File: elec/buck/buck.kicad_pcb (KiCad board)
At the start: 2 copper layers, 33 x 27.9 mm, 14 parts, among them J1 Conn_01x08, J2 Conn_01x08

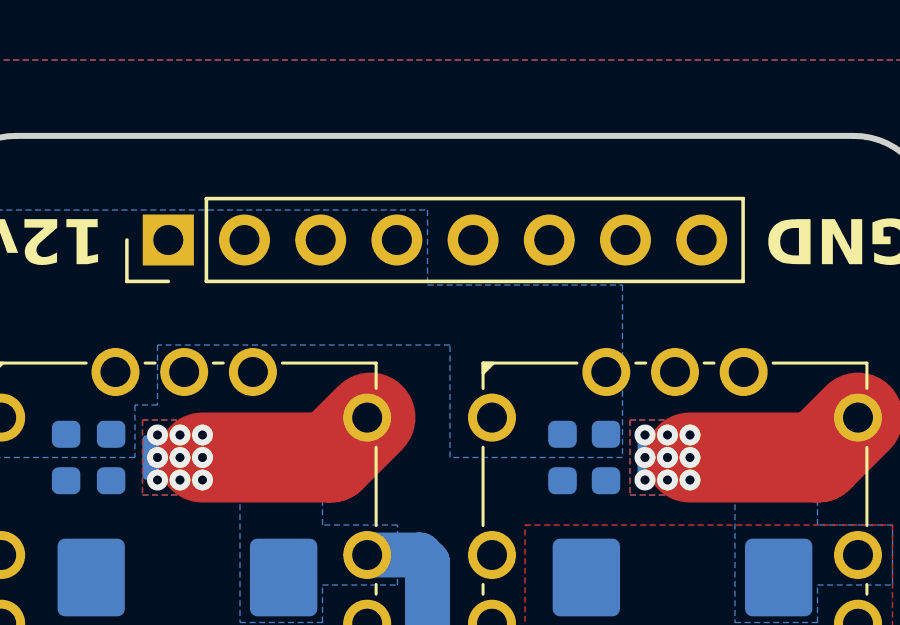
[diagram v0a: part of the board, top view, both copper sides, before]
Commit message: did buck pcba
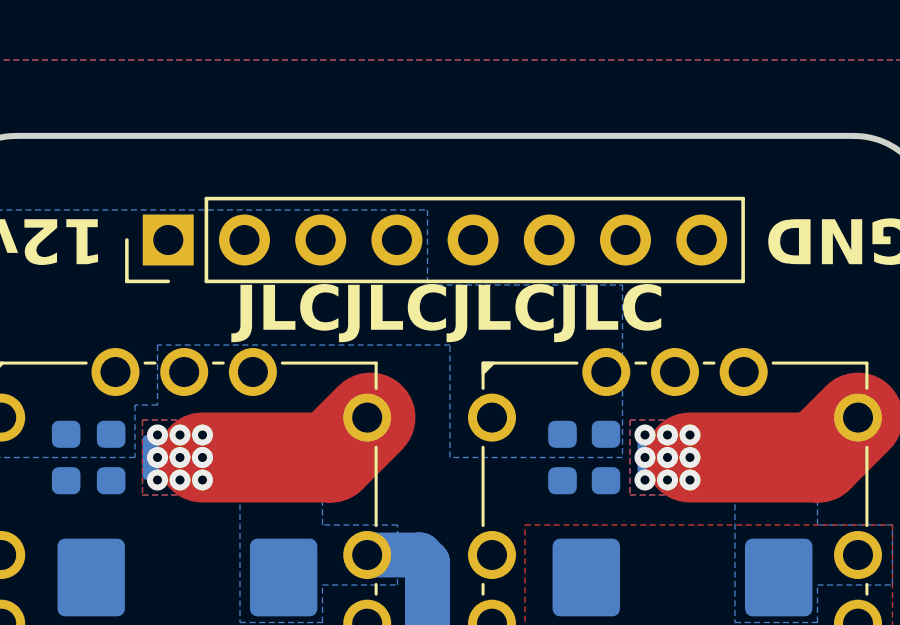
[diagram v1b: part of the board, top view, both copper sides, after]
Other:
- board text added: "JLCJLCJLCJLC"
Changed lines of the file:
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@@
 		(sheetname "/")
 		(sheetfile "buck.kicad_sch")
-		(attr smd)
+		(attr smd exclude_from_pos_files exclude_from_bom)
 		(fp_line
 			(start -6.3976 -6.3976)
@@
 		(sheetname "/")
 		(sheetfile "buck.kicad_sch")
-		(attr smd)
+		(attr smd exclude_from_pos_files exclude_from_bom)
 		(fp_line
 			(start -6.3976 -6.3976)
@@
 		(sheetname "/")
 		(sheetfile "buck.kicad_sch")
-		(attr through_hole)
+		(attr through_hole exclude_from_pos_files exclude_from_bom)
 		(fp_line
 			(start -1.38 -10.27)
@@
 		(sheetname "/")
 		(sheetfile "buck.kicad_sch")
-		(attr through_hole)
+		(attr through_hole exclude_from_pos_files exclude_from_bom)
 		(fp_line
 			(start -1.38 -10.27)
@@
 			)
 		)
+	)
+	(gr_text "JLCJLCJLCJLC\n"
+		(at 105.01 102.979999 0)
+		(layer "F.SilkS")
+		(effects
+			(font
+				(size 1.5 1.5)
+				(thickness 0.3)
+				(bold yes)
+			)
+		)

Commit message: prod: prod
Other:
- board text removed: "JLCJLCJLCJLC"
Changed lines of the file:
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@@
-		)
-	)
-	(gr_text "JLCJLCJLCJLC\n"
-		(at 105.01 102.979999 0)
-		(layer "F.SilkS")
-		(effects
-			(font
-				(size 1.5 1.5)
-				(thickness 0.3)
-				(bold yes)
-			)
 		)
 	)
